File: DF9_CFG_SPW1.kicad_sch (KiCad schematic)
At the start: 11 parts, among them J1 Picoblade_CFG, J2 DF9-41P-1V32, J3 DF9-CFG-SPW1, U7 TPS3828-33DBVR

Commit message: pre-order adjustments
DF9 connectors footprint adjusted.
Dimensions of board edges changed.
Placement of DF9 adjusted.
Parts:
- removed J2: DF9-41P-1V32, DataHub_Footprints:DF941P1V32, symbol DF9_connector_41:DF9-41P-1V32
- removed J3: DF9-CFG-SPW1, DataHub_Footprints:DF941P1V32, symbol DF9_connector_41:DF9-41P-1V32
- added J2, J3: DF9-41P-1V32, DataHub_Footprints:DF941P1V32, symbol DF9_real_custom:DF941S1V32
- renumbered D2 to D11, R10 to R22, R11 to R23, R12 to R24, R13 to R25, R20 to R26, R15 to R35, U7 to U11
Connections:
- net +1V7_IN: now also J3.1, J3.11, J3.3, J3.5, J3.7, J3.9
- net +3V3_IN: now also J3.19, J3.21, J3.23, J3.25, J3.27
- net +3V6_IN: now also J3.2, J3.4, J3.6, J3.8
- net +5V_IN: now also J3.14, J3.16
- net B0_01N_DF9: now also J2.21
- net B0_01P_DF9: now also J2.29
- net B0_02N_DF9: now also J2.34
- net B0_02P_DF9: now also J2.30
- net B0_03N_DF9: now also J2.26
- net B0_03P_DF9: now also J2.24
- net B0_04N_DF9: now also J2.36
- net B0_04P_DF9: now also J2.40
- net B0_05P_DF9: now also J2.19
- net B0_06N_DF9: now also J2.27
- net B0_06P_DF9: now also J2.18
- net B0_07N_DF9: now also J2.33
- net B0_07P_DF9: now also J2.20
- net B0_08P_DF9: now also J2.22
- net B0_09N_DF9: now also J2.17
- net B0_09P_DF9: now also J2.25
- net B0_10N_DF9: now also J2.28
- net B0_10P_DF9: now also J2.37
- net B0_11P_DF9: now also J2.15
- net B5_03N_DF9: now also J3.38
- net B5_03P_DF9: now also J3.40
- net B5_04N_DF9: now also J3.39
- net B5_07N_DF9: now also J3.37
- net B5_08N_DF9: now also J3.34
- net B5_08P_DF9: now also J3.36
- net B5_09N_DF9: now also J3.41
- net B5_10N_DF9: now also J3.33
- net B5_10P_DF9: now also J3.35
- net B5_11N_DF9: now also J3.30
- net B5_11P_DF9: now also J3.32
- net B5_12N_DF9: now also J3.26
- net B5_12P_DF9: now also J3.28
- net B5_13N_DF9: now also J3.31
- net GND: now also J2.1, J2.10, J2.13, J2.16, J2.2, J2.23, J2.31, J2.32, J2.35, J2.38, J2.39, J2.4, J2.41, J2.7, J2.MP1, J2.MP2, J3.10, J3.12, J3.13, J3.15, J3.17, J3.18, J3.20, J3.22, J3.24, J3.29, J3.MP1, J3.MP2
- net SPW1_DIN_N: now also J2.8
- net SPW1_DIN_P: now also J2.6
- net SPW1_DOUT_N: now also J2.11
- net SPW1_DOUT_P: now also J2.9
- net SPW1_SIN_N: now also J2.5
- net SPW1_SIN_P: now also J2.3
- net SPW1_SOUT_N: now also J2.14
- net SPW1_SOUT_P: now also J2.12

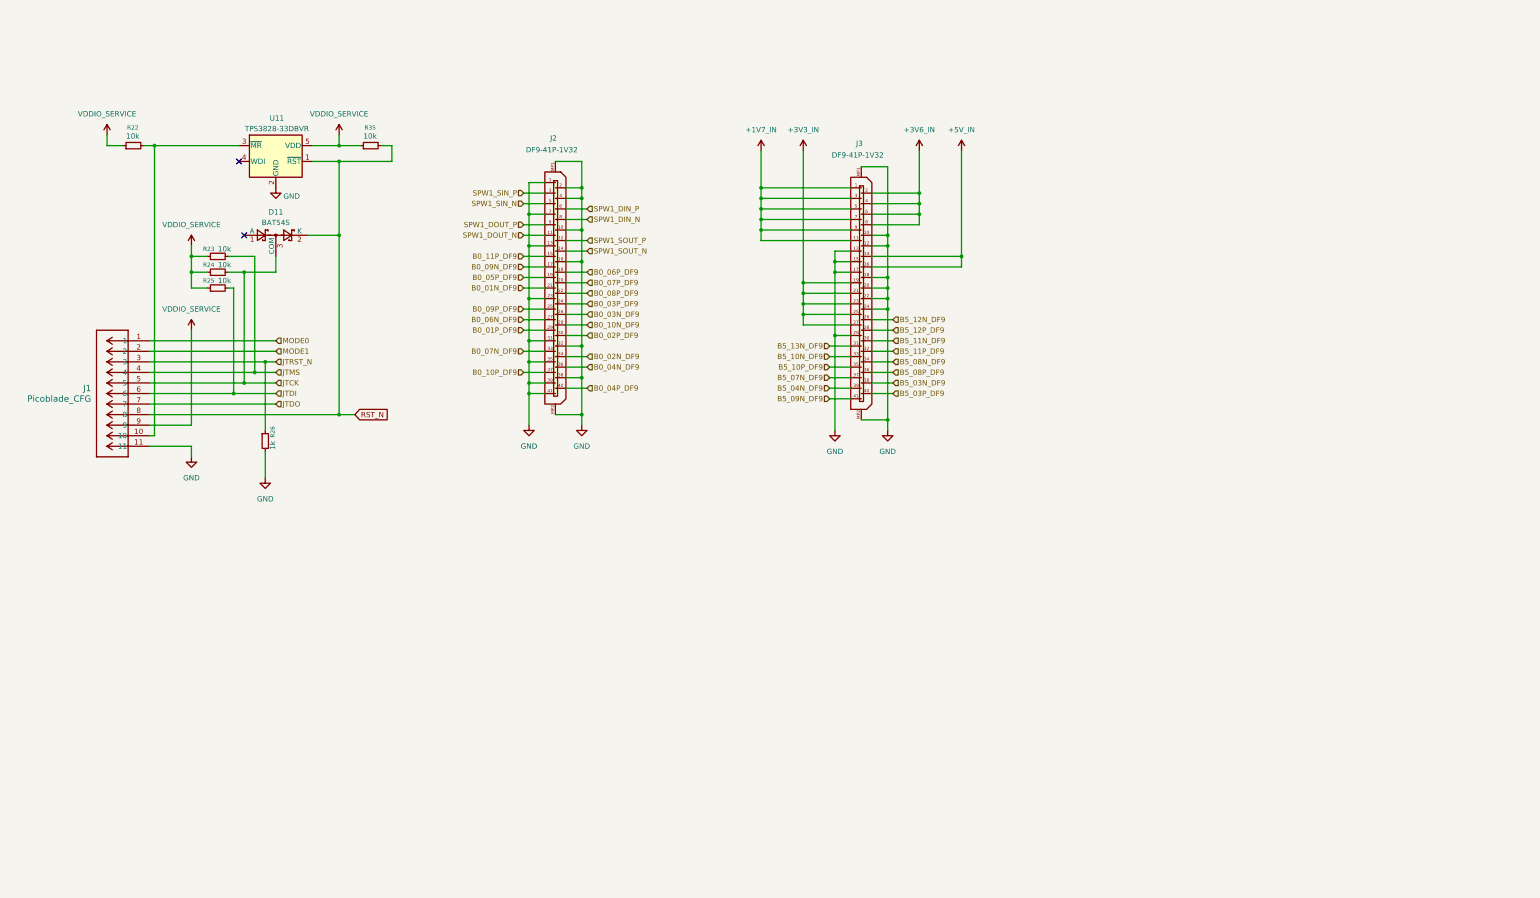
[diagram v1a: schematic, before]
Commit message: pre order adjustments. Board symmetry
adjusted little things brought up by DFM checker of JLCPCB. Board's edges fully symmetrical on y axis. 2mm shift on x axis of the DF9s maintained
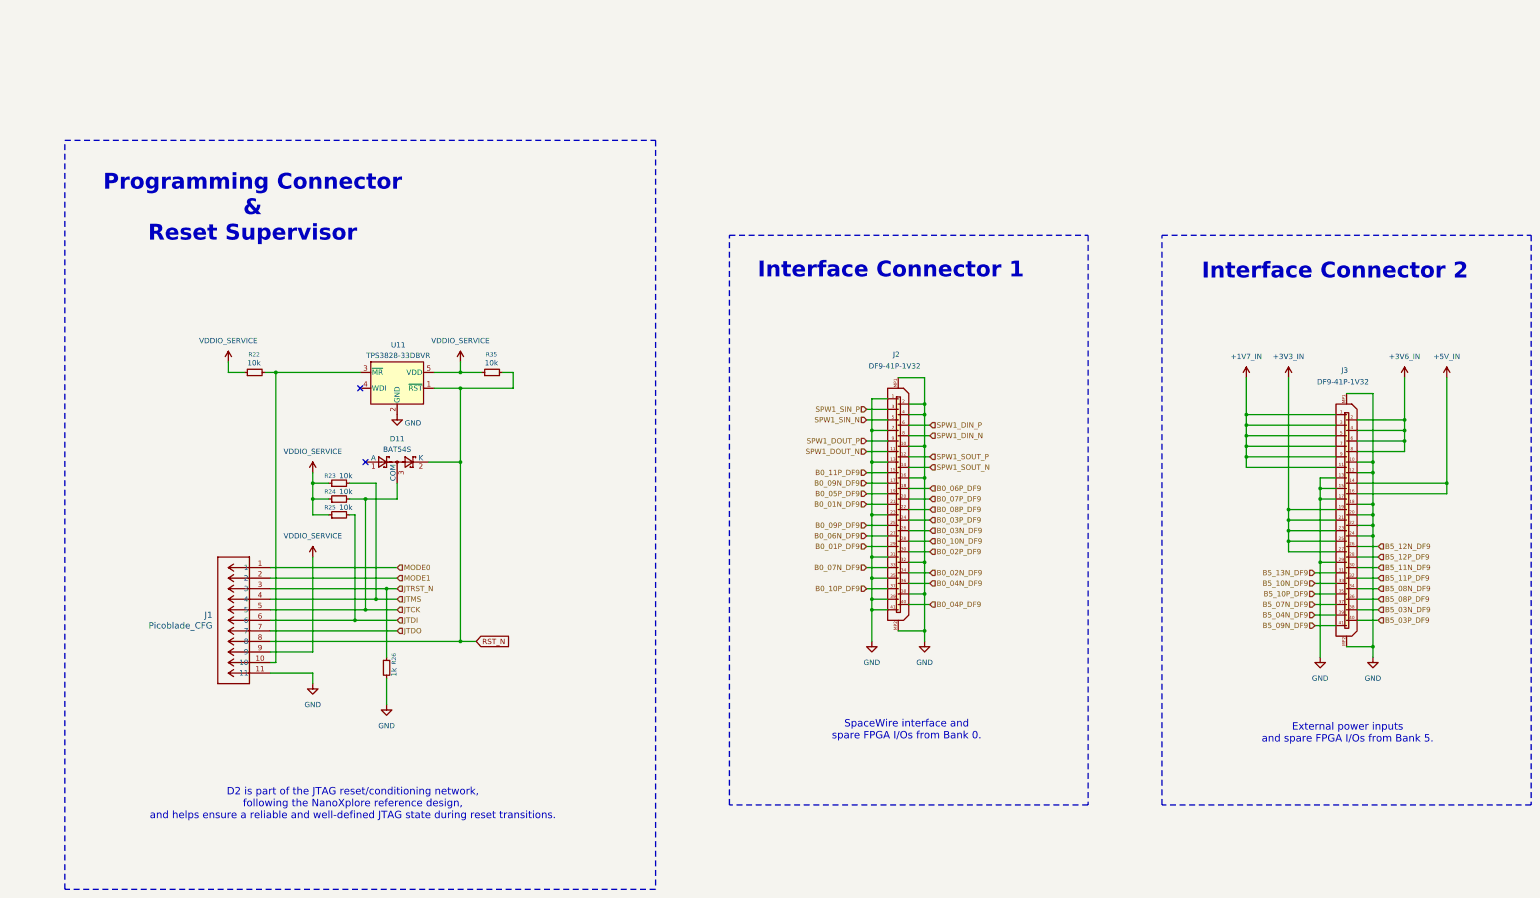
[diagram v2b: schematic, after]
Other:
- note added: "D2 is part of the JTAG reset/conditioning network, following the NanoXplore reference design, and helps ensure a reliable and well-defined JTAG state during reset transitions."
- note added: "External power inputs and spare FPGA I/Os from Bank 5."
- note added: "Interface Connector 1"
- note added: "Interface Connector 2"
- note added: "Programming Connector & Reset Supervisor"
- note added: "SpaceWire interface and spare FPGA I/Os from Bank 0."
- moved on the sheet: D11, J1, J2, J3, R22, R23, R24, R25, R26, R35, U11
